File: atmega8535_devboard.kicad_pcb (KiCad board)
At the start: 2 copper layers, 38 parts, among them IC1 ATMEGA8535-P, Q1 BC211-10, Q2 BC211-10, Q3 BC211-10, X1 16MHz

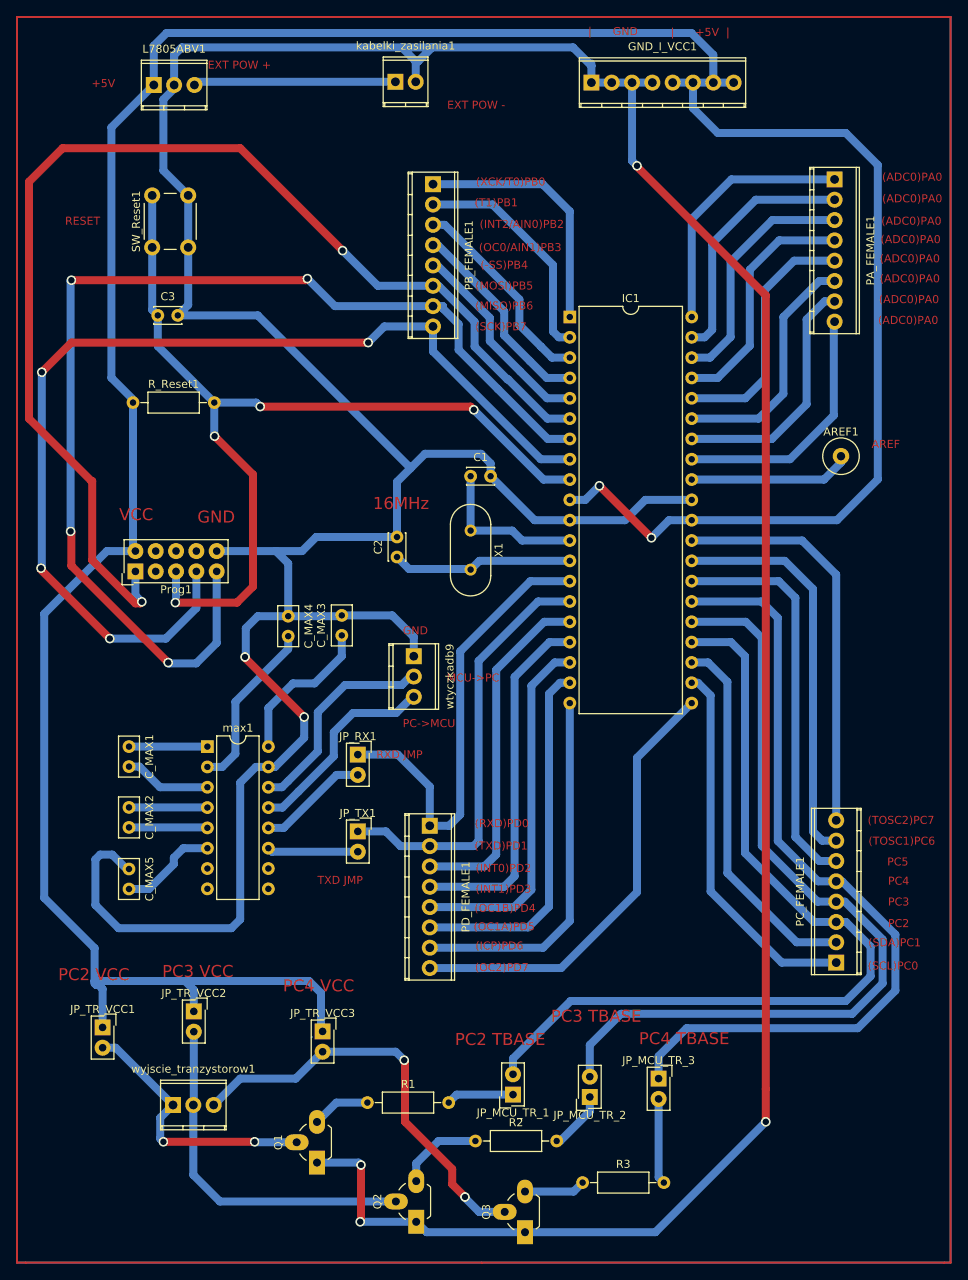
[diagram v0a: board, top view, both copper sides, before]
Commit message: make the board smaller
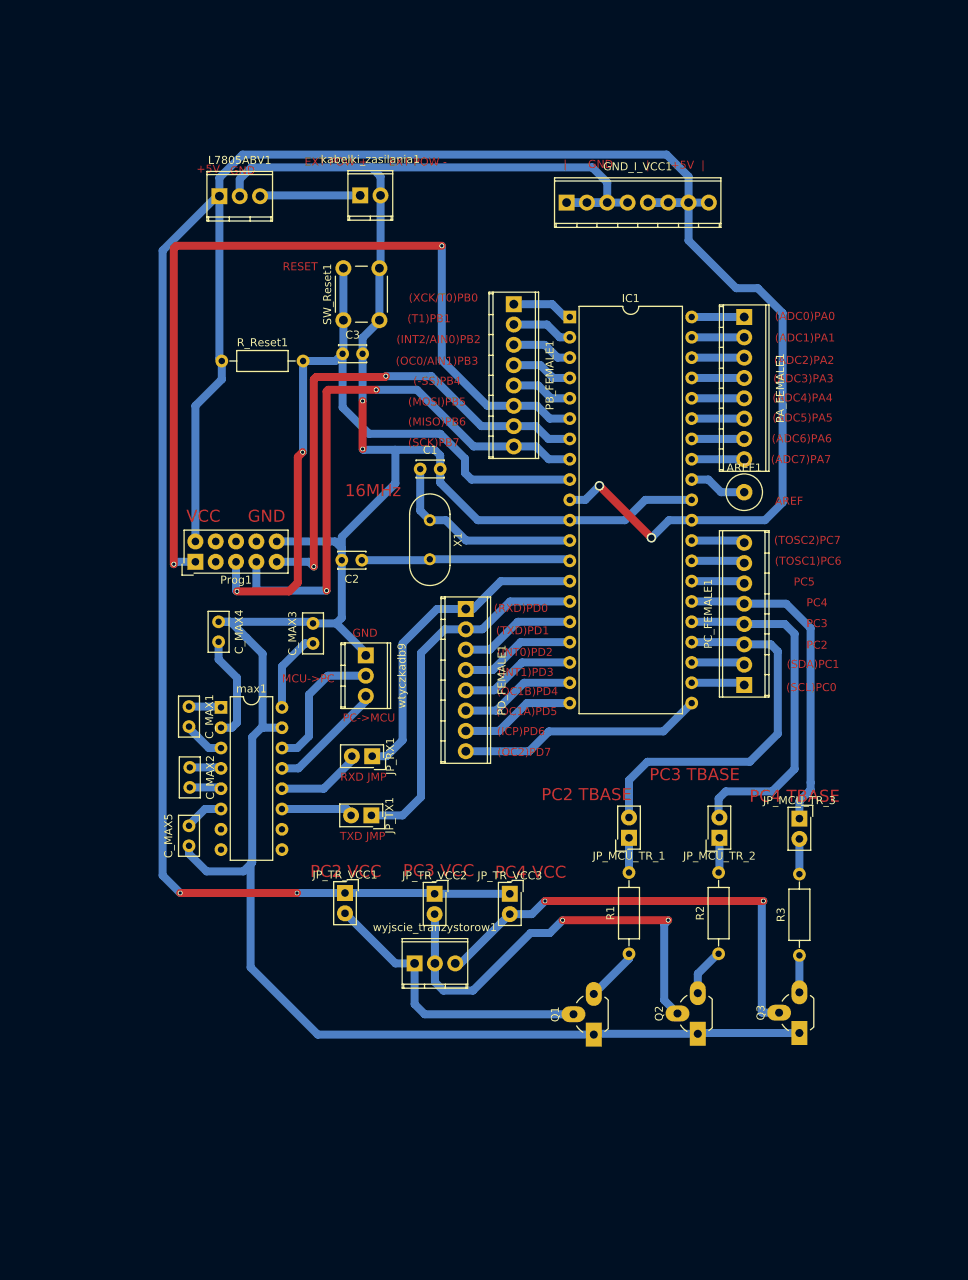
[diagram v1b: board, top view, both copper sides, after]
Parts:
- moved Q3 42.4 mm to (112.0, 144.5)
- moved Q2 42.3 mm to (99.3, 144.6)
- moved R3 39.3 mm to (112.0, 134.8), turned to 90 degrees
- moved R2 38.4 mm to (101.9, 134.6), turned to 90 degrees
- moved Q1 38.1 mm to (86.3, 144.7)
- moved R1 37.6 mm to (90.7, 134.6), turned to 90 degrees
- moved JP_MCU_TR_3 37.0 mm to (112.0, 117.7)
- moved PC_FEMALE1 36.6 mm to (105.1, 101.0)
- moved JP_MCU_TR_2 36.2 mm to (102.0, 120.1)
- moved JP_MCU_TR_1 35.2 mm to (90.7, 120.1)
- moved wyjscie_tranzystorow1 35.0 mm to (63.9, 135.8)
- moved JP_TR_VCC1 34.6 mm to (55.2, 127.0)
- moved JP_TR_VCC2 33.5 mm to (66.4, 127.1)
- moved JP_TR_VCC3 29.0 mm to (75.8, 127.1)
- moved PD_FEMALE1 27.5 mm to (70.3, 91.5)
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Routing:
- net (no net): track 1089.7 -> 0.00 mm
- net GND: track 532.5 -> 334.5 mm, vias 6 -> 2
- net Net-(IC1-Pad7): track 141.7 -> 63.7 mm, vias 4 -> 2
- net Net-(IC1-Pad26): track 102.0 -> 40.6 mm
- net Net-(IC1-Pad25): track 104.8 -> 43.8 mm
- net Net-(IC1-Pad8): track 131.8 -> 71.4 mm, vias 4 -> 2
- net Net-(IC1-Pad24): track 107.3 -> 47.2 mm
- net Net-(IC1-Pad29): track 51.1 -> 6.68 mm
- net Net-(IC1-Pad28): track 50.3 -> 6.68 mm
- net Net-(IC1-Pad27): track 50.2 -> 6.68 mm
- net Net-(IC1-Pad22): track 46.9 -> 6.68 mm
- net Net-(IC1-Pad23): track 46.6 -> 6.68 mm
- net Net-(GND_I_VCC1-Pad5): track 371.4 -> 332.1 mm, vias 2 -> 4
- net Net-(IC1-Pad6): track 148.4 -> 109.3 mm
- net Net-(IC1-Pad20): track 46.1 -> 14.4 mm
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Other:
- board text added: "(ADC1)PA1"
- board text added: "(ADC2)PA2"
- board text added: "(ADC3)PA3"
- board text added: "(ADC4)PA4"
- board text added: "(ADC5)PA5"
- board text added: "(ADC6)PA6"
- board text added: "(ADC7)PA7"

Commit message: add more ground
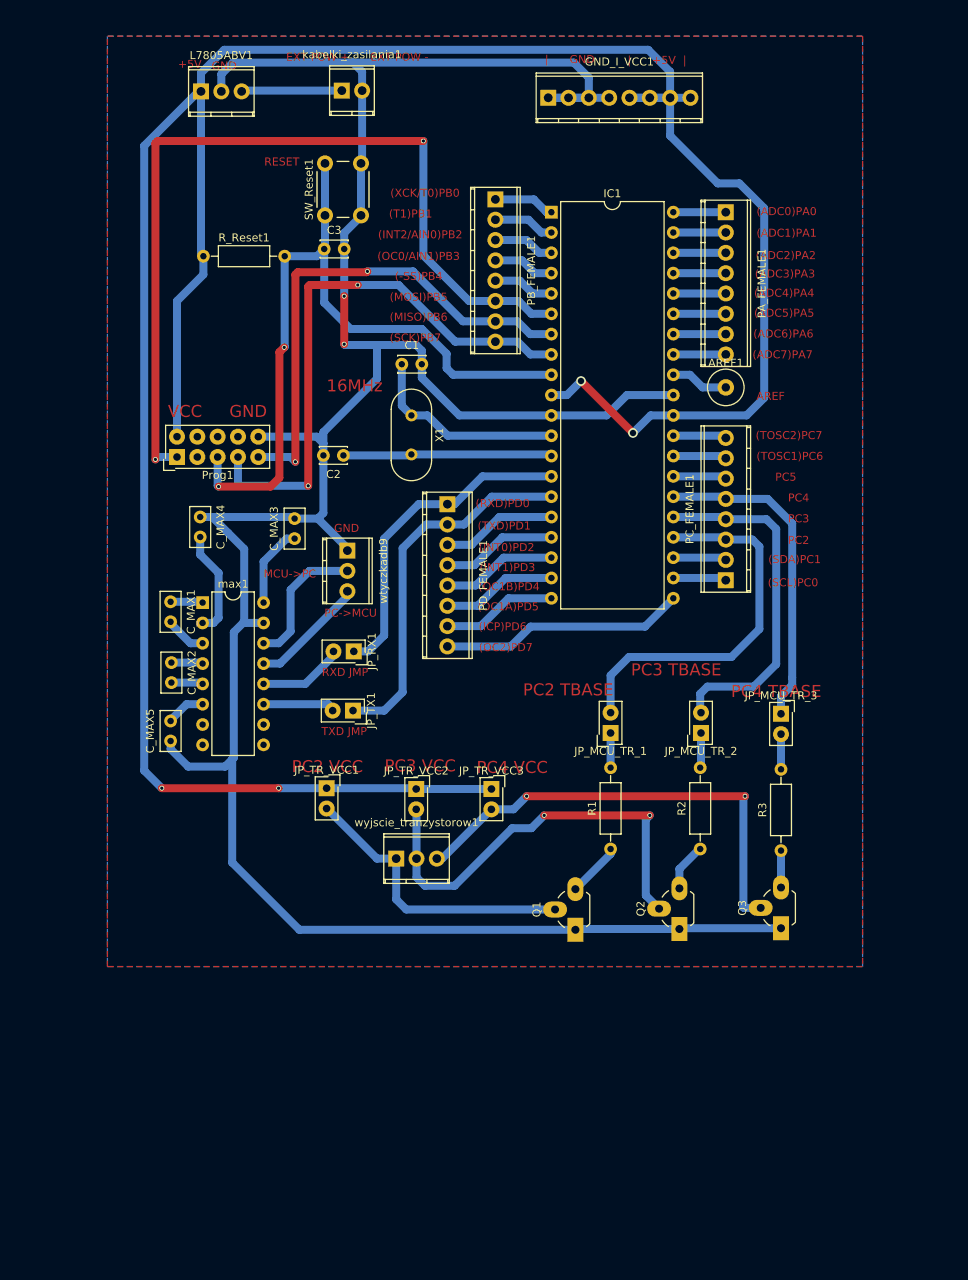
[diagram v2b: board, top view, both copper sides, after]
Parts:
- moved C_MAX1 13.3 mm to (33.4, 90.6)
- moved JP_RX1 13.3 mm to (56.3, 96.8)
- moved AREF1 13.3 mm to (102.8, 63.8)
- moved C2 13.3 mm to (55.0, 72.3)
- moved JP_MCU_TR_3 13.3 mm to (109.7, 104.6)
- moved R3 13.3 mm to (109.7, 121.7)
- moved X1 13.3 mm to (63.5, 67.3)
- moved wyjscie_tranzystorow1 13.3 mm to (61.6, 122.7)
- moved GND_I_VCC1 13.3 mm to (80.6, 27.6)
- moved C1 13.3 mm to (62.3, 60.9)
- moved C3 13.3 mm to (52.6, 46.5)
- moved IC1 13.3 mm to (81.0, 41.9)
- moved L7805ABV1 13.3 mm to (37.2, 26.8)
- moved PA_FEMALE1 13.3 mm to (102.8, 41.9)
- moved PB_FEMALE1 13.3 mm to (74.0, 40.3)
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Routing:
- added copper zone on B.Cu, net GND
- added copper zone on F.Cu, net GND
